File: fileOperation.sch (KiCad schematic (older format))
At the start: 19 parts, among them IC1 XC2C256-VQ100, J1 ALU_JTAG, J4 UnusedPins_Connector, J5 ALU_PINS, U28 TPS7A0518PDBZR, U30 SN74LVC8T245DW, U32 SN74AVC4T245D

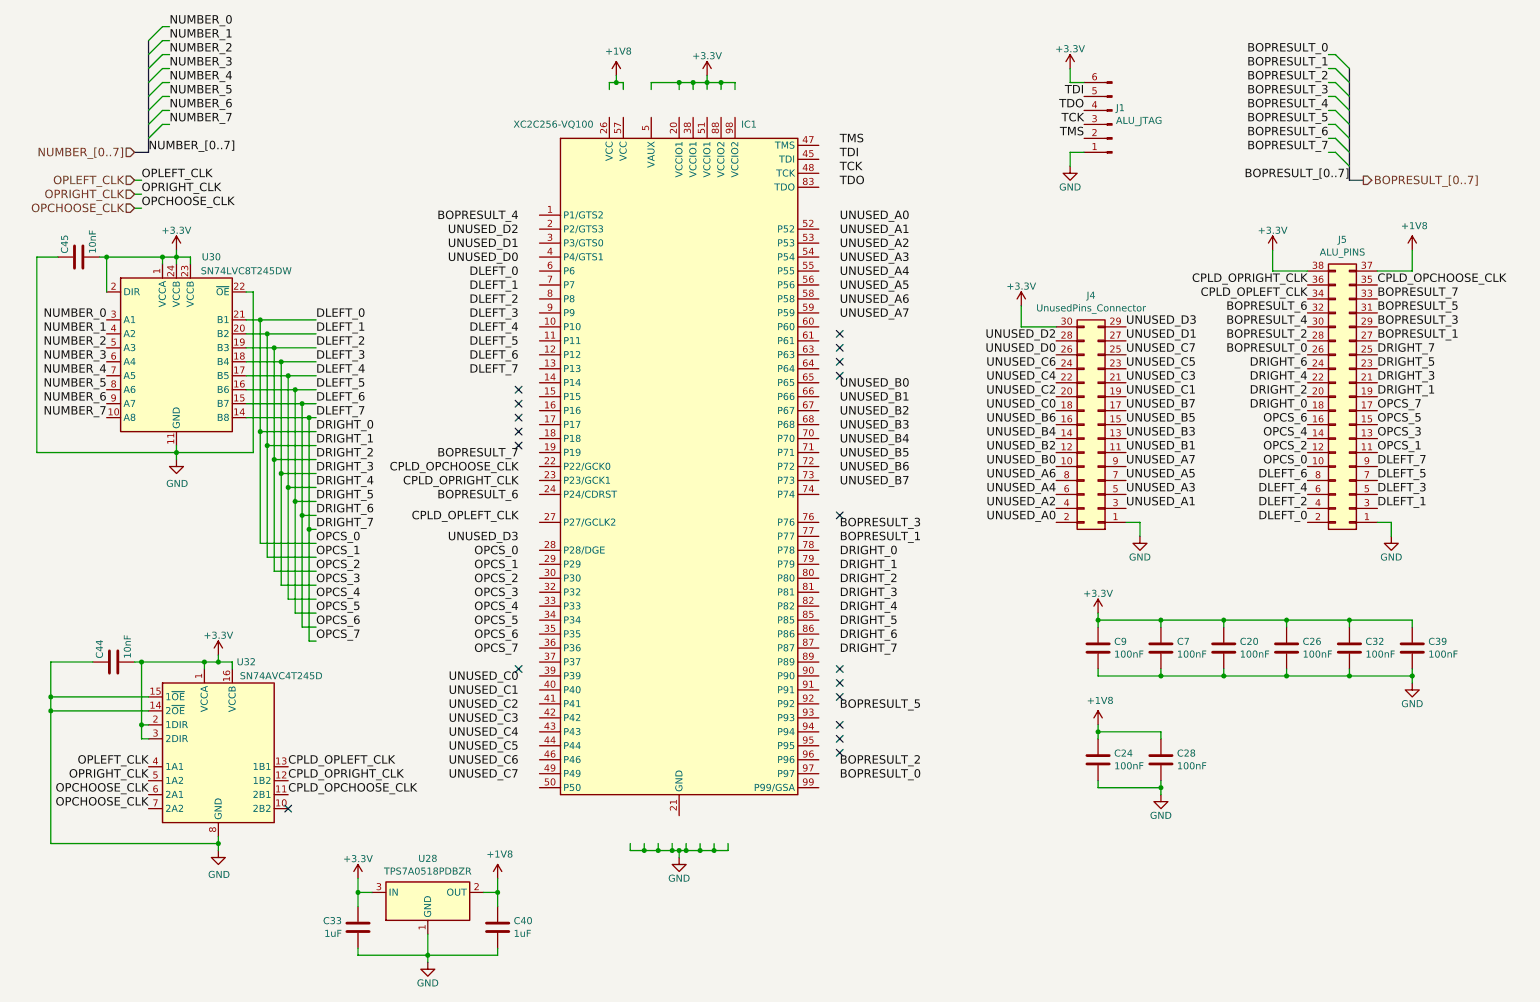
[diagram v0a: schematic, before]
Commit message: Apply new symbol for XC2C256-VQ100 #5
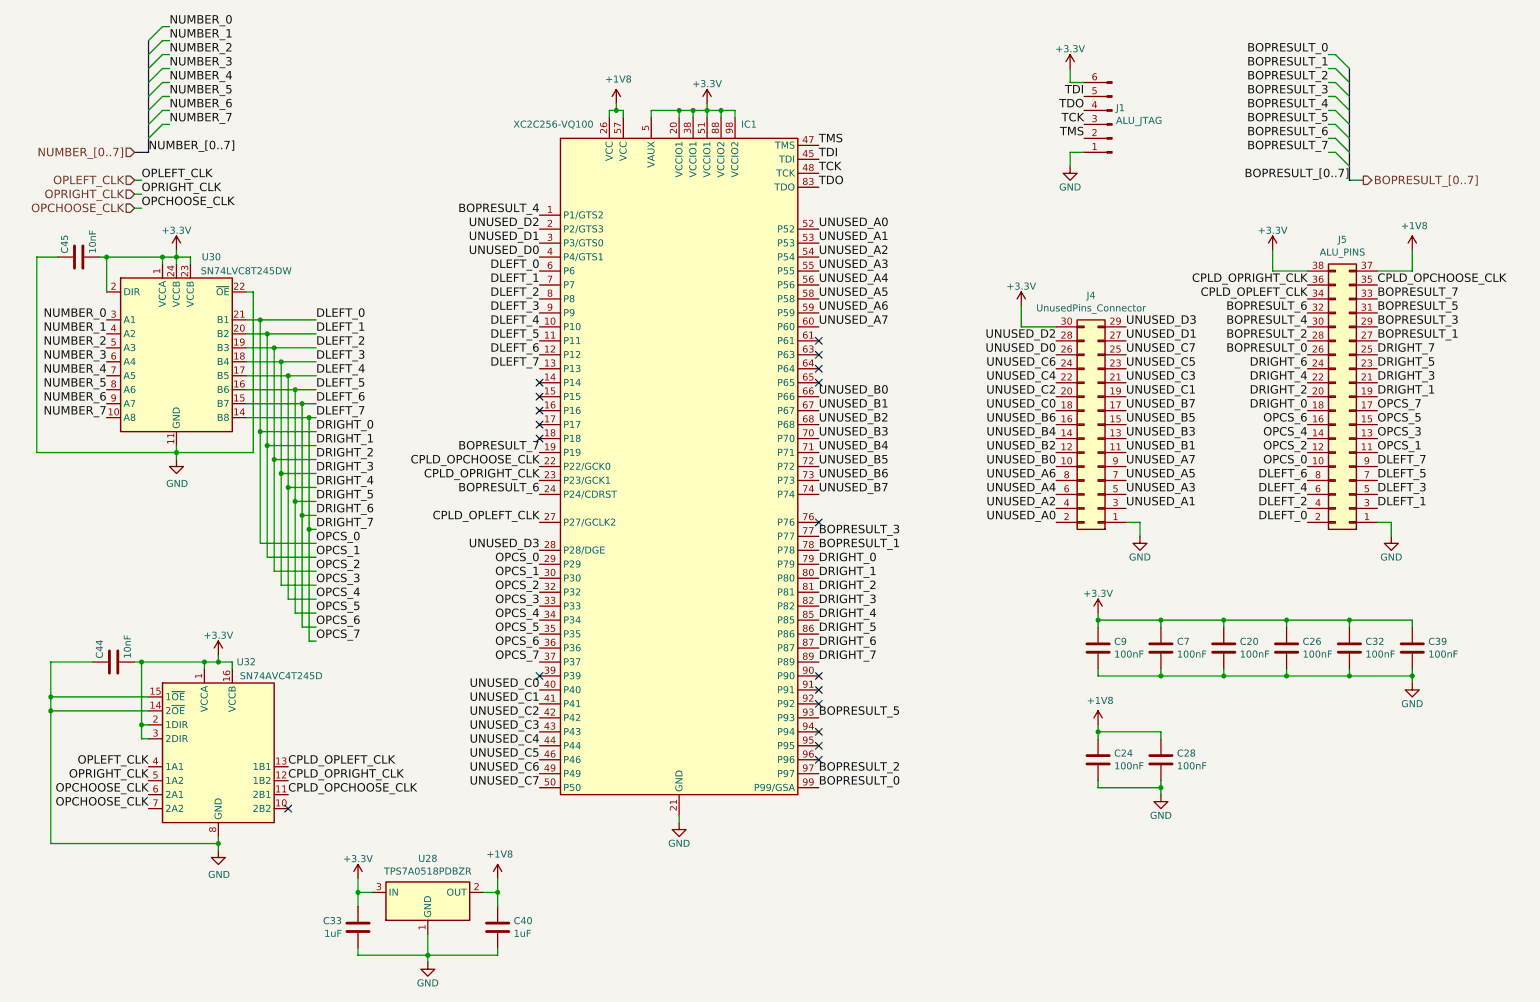
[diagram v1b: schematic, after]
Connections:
- wire segments 196 -> 180
